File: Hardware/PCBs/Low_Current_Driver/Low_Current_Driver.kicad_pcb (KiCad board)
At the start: 4 copper layers, 160 x 99.5 mm, 194 parts, among them J1 Conn_01x02, J2 RJ45, J3 Screw_Terminal_01x04, J4 Conn_02x07_Odd_Even, J5 Channel 3, J6 Channel 2, J7 Channel 1, J8 MS548-10F, J9 Conn_01x02, Q1 Si4447ADY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

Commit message: Switch to common footprint library
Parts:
- J1: footprint Dummy_conn_01x02:PinSocket_1x02_P1.00mm_Vertical_CUSTOM_CYD -> vernier_current_driver:PinSocket_1x02_P1.00mm_Vertical_CUSTOM_CYD
- J8: footprint MS548-10F:MS548-10C -> vernier_current_driver:MS548-10C
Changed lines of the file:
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@@
     )
   )
-  (module MS548-10F:MS548-10C (layer F.Cu)
+  (module vernier_current_driver:MS548-10C (layer F.Cu)
     (at 111.6425 82.27 90)
     (fp_text reference J8 (at 0 2.83 90) (layer F.SilkS)
@@
       (net 9 GND))
   )
-  (module Dummy_conn_01x02:PinSocket_1x02_P1.00mm_Vertical_CUSTOM_CYD (layer F.Cu)
+  (module vernier_current_driver:PinSocket_1x02_P1.00mm_Vertical_CUSTOM_CYD (layer F.Cu)
     (at 115.5065 84.1375)
     (descr "Through hole straight socket strip, 1x02, 1.00mm pitch, single row (https://gct.co/files/drawings/bc065.pdf), script generated")

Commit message: Bump version to 1.1.0
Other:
- board text added: "Vernier LCD v1.1.0 April 2021 Designer: Marcin Mrozowski EQOP"
- board text removed: "Vernier LCD Rev 1.0D April 2021 Designer: Marcin Mrozowski EQOP"
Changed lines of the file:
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@@
     (title "\"Vernier Vamp\" Coil Driver - 2mA")
     (date 2020-05-12)
-    (rev 1.0B)
+    (rev 1.1.0)
     (company "Strathclyde University")
     (comment 1 "Designed by: Marcin Mrozowski")
@@
     (arrow2b (pts (xy 32.9 157.149999) (xy 34.026504 156.563578)))
   )
-  (gr_text "Vernier LCD\nRev 1.0D\nApril 2021\nDesigner: Marcin Mrozowski\nEQOP" (at 151.65 128) (layer B.SilkS)
+  (gr_text "Vernier LCD\nv1.1.0\nApril 2021\nDesigner: Marcin Mrozowski\nEQOP" (at 151.65 128) (layer B.SilkS)
     (effects (font (size 1.5 1.5) (thickness 0.3)) (justify mirror))
   )
@@
     (effects (font (size 1.5 1.5) (thickness 0.3)))
   )
-  (gr_text "Vernier LCD\nRev 1.0D\nApril 2021\nDesigner: Marcin Mrozowski\nEQOP" (at 151.6 127.95) (layer F.SilkS)
+  (gr_text "Vernier LCD\nv1.1.0\nApril 2021\nDesigner: Marcin Mrozowski\nEQOP" (at 151.6 127.95) (layer F.SilkS)
     (effects (font (size 1.5 1.5) (thickness 0.3)))
   )

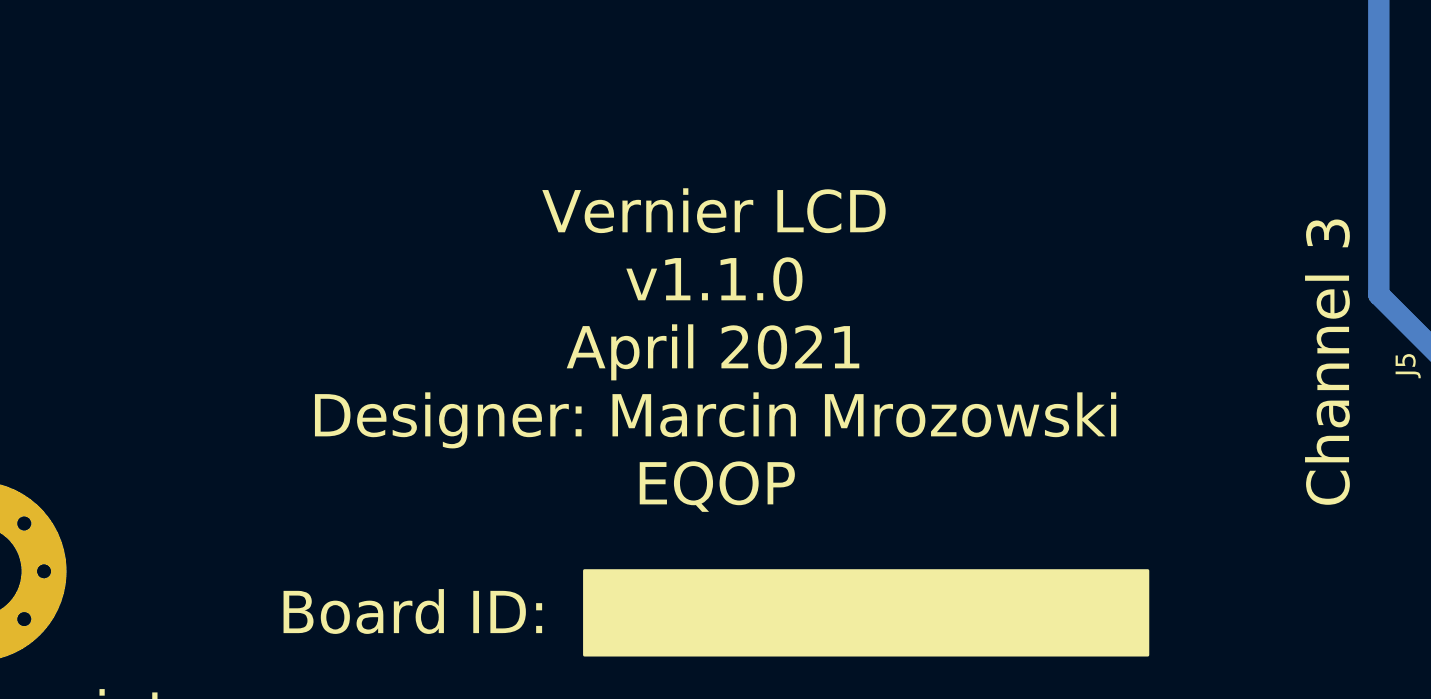
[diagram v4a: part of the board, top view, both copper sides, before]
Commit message: Add repo link to silkscreen
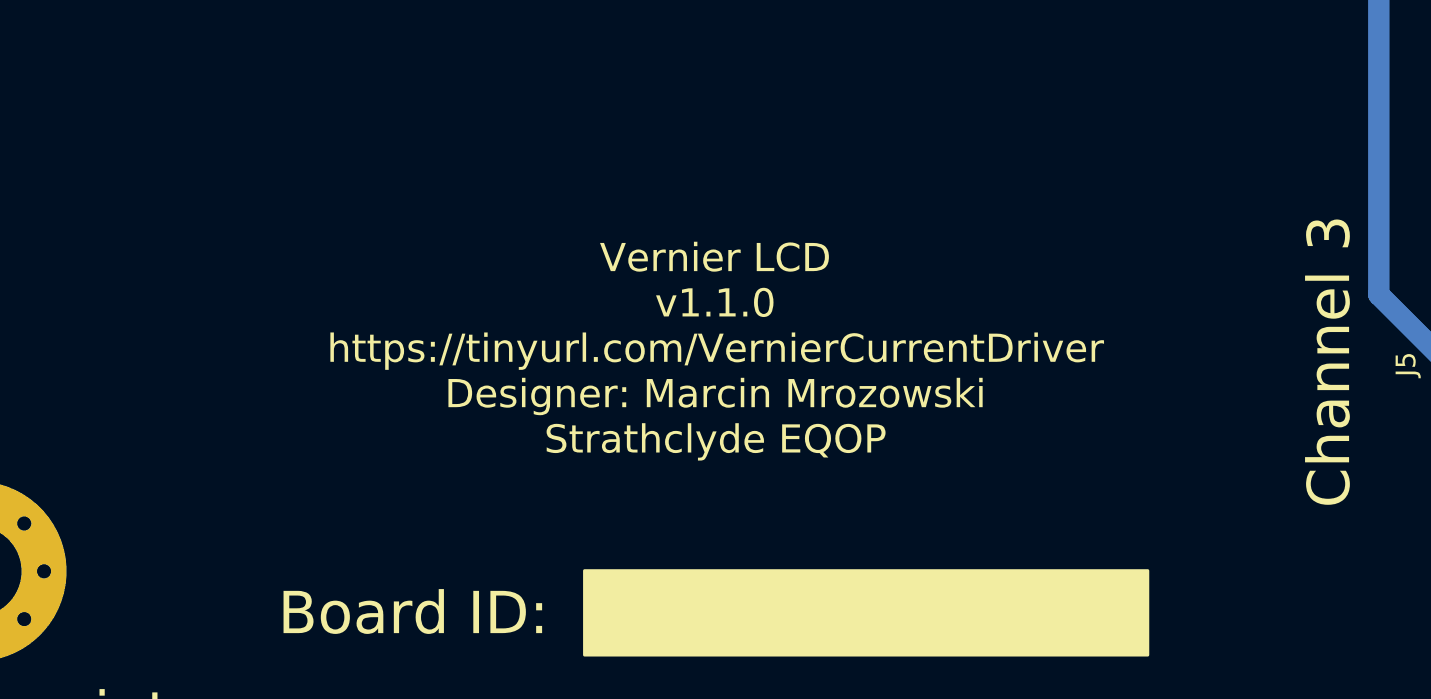
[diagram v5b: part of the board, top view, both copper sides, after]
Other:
- board text added: "Vernier LCD v1.1.0 https://tinyurl.com/VernierCurrentDriver Designer: Marcin Mrozowski Strathclyde EQOP"
- board text removed: "Vernier LCD v1.1.0 April 2021 Designer: Marcin Mrozowski EQOP"
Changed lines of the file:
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@@
     (arrow2b (pts (xy 32.9 157.149999) (xy 34.026504 156.563578)))
   )
-  (gr_text "Vernier LCD\nv1.1.0\nApril 2021\nDesigner: Marcin Mrozowski\nEQOP" (at 151.65 128) (layer B.SilkS)
-    (effects (font (size 1.5 1.5) (thickness 0.3)) (justify mirror))
+  (gr_text "Vernier LCD\nv1.1.0\nhttps://tinyurl.com/VernierCurrentDriver\nDesigner: Marcin Mrozowski\nStrathclyde EQOP" (at 151.65 128) (layer B.SilkS)
+    (effects (font (size 1 1) (thickness 0.15)) (justify mirror))
   )
   (gr_text "Board ID:\n" (at 161.9 137.45) (layer B.SilkS)
@@
     (effects (font (size 1.5 1.5) (thickness 0.3)))
   )
-  (gr_text "Vernier LCD\nv1.1.0\nApril 2021\nDesigner: Marcin Mrozowski\nEQOP" (at 151.6 127.95) (layer F.SilkS)
-    (effects (font (size 1.5 1.5) (thickness 0.3)))
+  (gr_text "Vernier LCD\nv1.1.0\nhttps://tinyurl.com/VernierCurrentDriver\nDesigner: Marcin Mrozowski\nStrathclyde EQOP" (at 151.6 127.95) (layer F.SilkS)
+    (effects (font (size 1 1) (thickness 0.15)))
   )
   (gr_poly (pts (xy 166.95 135.825) (xy 146.95 135.825) (xy 146.95 138.825) (xy 166.95 138.825)) (layer F.SilkS) (width 0.1))
